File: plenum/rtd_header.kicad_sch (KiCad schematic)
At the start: 1 part, among them J3 Conn_03x20_MountingPin

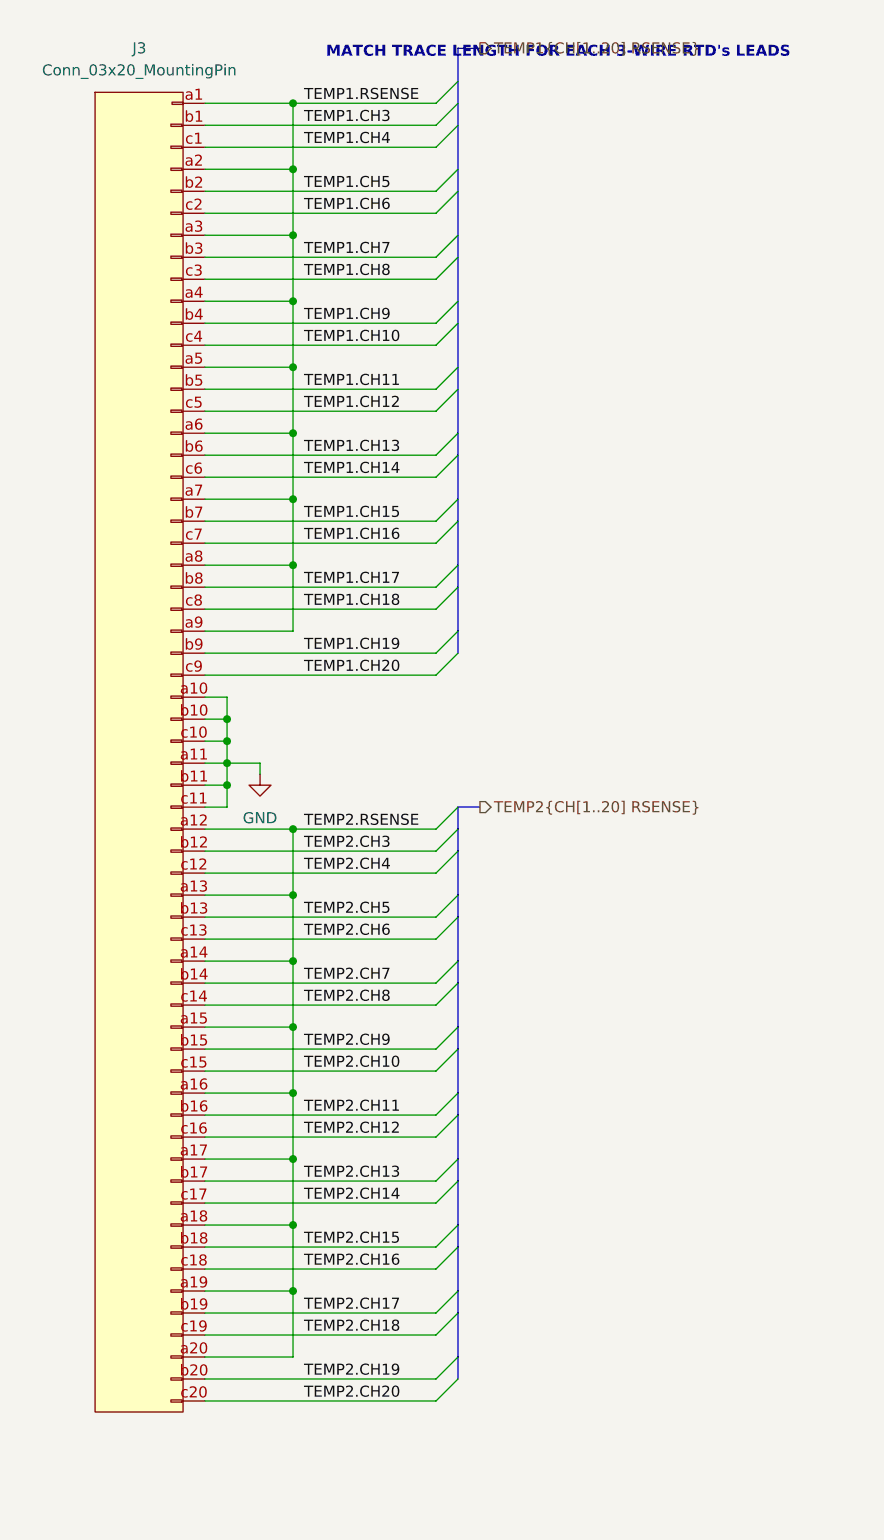
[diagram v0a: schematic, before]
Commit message: adding housekeeping board
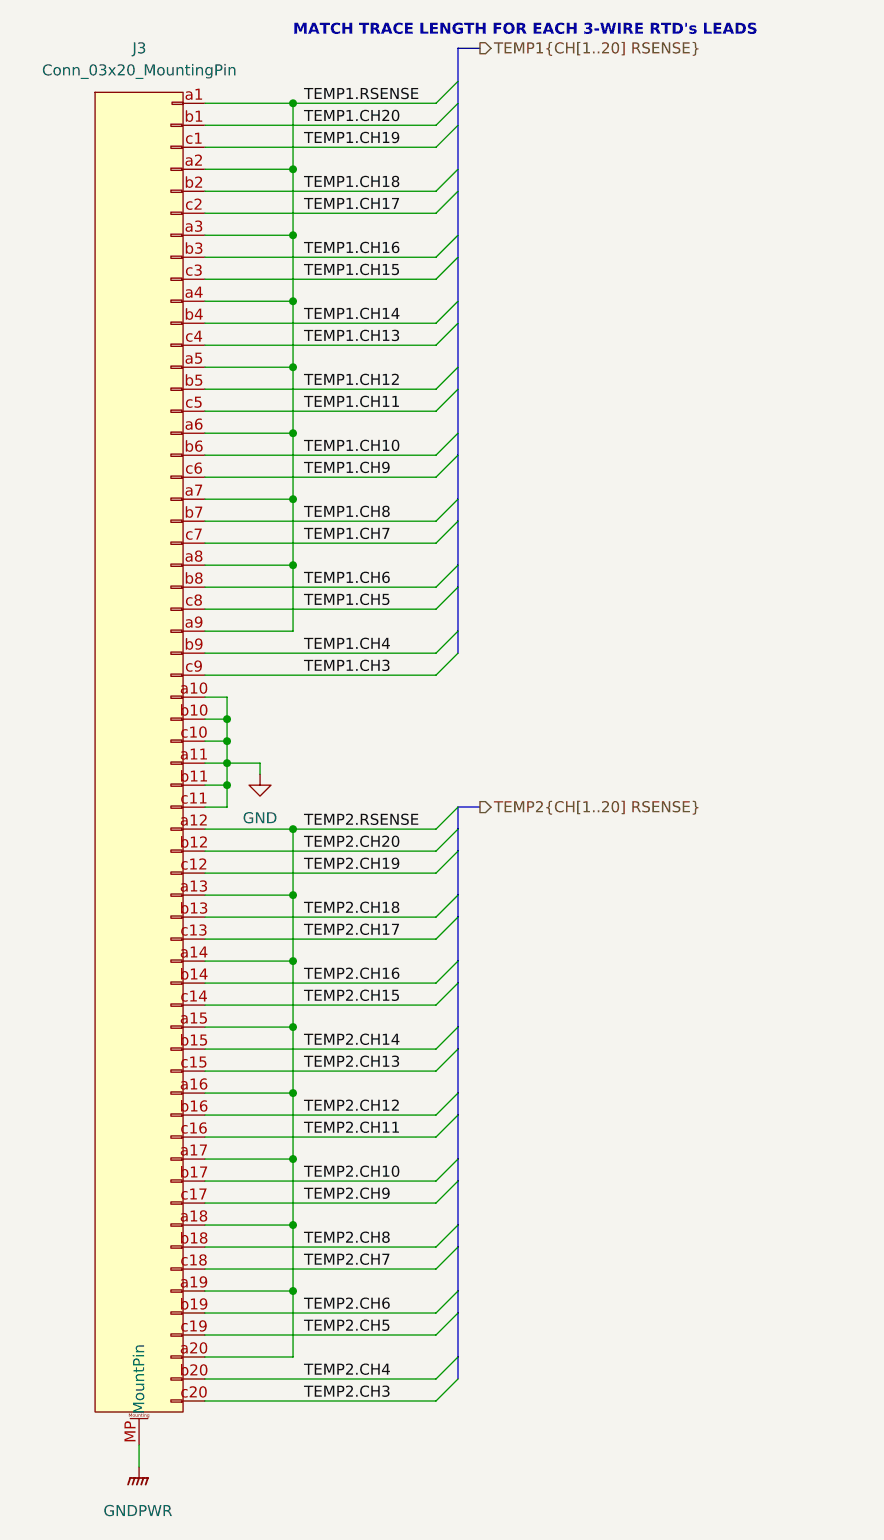
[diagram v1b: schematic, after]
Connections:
- net TEMP1.CH10: now also J3.b6; no longer J3.c4
- net TEMP1.CH11: now also J3.c5; no longer J3.b5
- net TEMP1.CH12: now also J3.b5; no longer J3.c5
- net TEMP1.CH13: now also J3.c4; no longer J3.b6
- net TEMP1.CH14: now also J3.b4; no longer J3.c6
- net TEMP1.CH15: now also J3.c3; no longer J3.b7
- net TEMP1.CH16: now also J3.b3; no longer J3.c7
- net TEMP1.CH17: now also J3.c2; no longer J3.b8
- net TEMP1.CH18: now also J3.b2; no longer J3.c8
- net TEMP1.CH19: now also J3.c1; no longer J3.b9
- net TEMP1.CH20: now also J3.b1; no longer J3.c9
- net TEMP1.CH3: now also J3.c9; no longer J3.b1
- net TEMP1.CH4: now also J3.b9; no longer J3.c1
- net TEMP1.CH5: now also J3.c8; no longer J3.b2
- net TEMP1.CH6: now also J3.b8; no longer J3.c2
- net TEMP1.CH7: now also J3.c7; no longer J3.b3
- net TEMP1.CH8: now also J3.b7; no longer J3.c3
- net TEMP1.CH9: now also J3.c6; no longer J3.b4
- net TEMP2.CH10: now also J3.b17; no longer J3.c15
- net TEMP2.CH11: now also J3.c16; no longer J3.b16
- net TEMP2.CH12: now also J3.b16; no longer J3.c16
- net TEMP2.CH13: now also J3.c15; no longer J3.b17
- net TEMP2.CH14: now also J3.b15; no longer J3.c17
- net TEMP2.CH15: now also J3.c14; no longer J3.b18
- net TEMP2.CH16: now also J3.b14; no longer J3.c18
- net TEMP2.CH17: now also J3.c13; no longer J3.b19
- net TEMP2.CH18: now also J3.b13; no longer J3.c19
- net TEMP2.CH19: now also J3.c12; no longer J3.b20
- net TEMP2.CH20: now also J3.b12; no longer J3.c20
- net TEMP2.CH3: now also J3.c20; no longer J3.b12
- net TEMP2.CH4: now also J3.b20; no longer J3.c12
- net TEMP2.CH5: now also J3.c19; no longer J3.b13
- net TEMP2.CH6: now also J3.b19; no longer J3.c13
- net TEMP2.CH7: now also J3.c18; no longer J3.b14
- net TEMP2.CH8: now also J3.b18; no longer J3.c14
- net TEMP2.CH9: now also J3.c17; no longer J3.b15
- new net GNDPWR: J3.MP (MountPin)
